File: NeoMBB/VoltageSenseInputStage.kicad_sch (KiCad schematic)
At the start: 8 parts

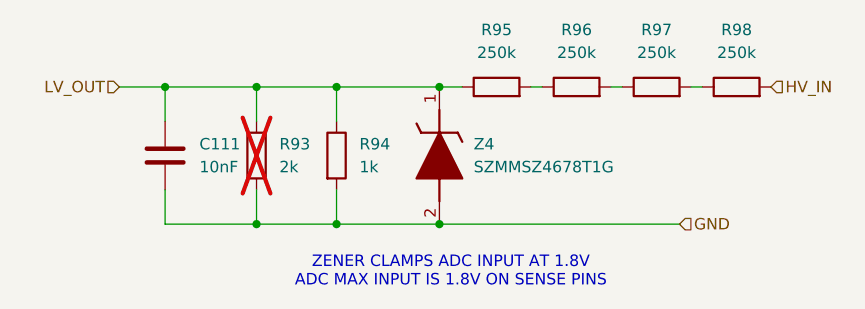
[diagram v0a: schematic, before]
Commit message: Probed Zero wiring harness
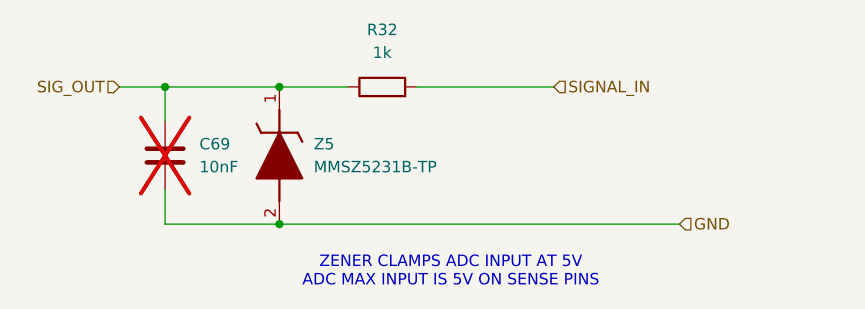
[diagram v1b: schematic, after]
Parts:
- removed R93: 2k, Resistor_SMD:R_1210_3225Metric_Pad1.30x2.65mm_HandSolder, symbol Device:R
- removed R95, R96, R97, R98: 250k, Resistor_SMD:R_1210_3225Metric_Pad1.30x2.65mm_HandSolder, symbol Device:R
- removed Z4: SZMMSZ4678T1G, InverterCom:SOD3716X135N, symbol InverterCom:SZMMSZ4678T1G
- added Z5: MMSZ5231B-TP, SOD3716X135N, symbol InverterCom:MMSZ5231B-TP
- C69: renamed from C111; now not fitted
- renumbered R94 to R32
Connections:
- net GND: now also Z5.2 (A); no longer R32.2
- net LV_OUT renamed SIG_OUT
- net SIG_OUT: now also Z5.1 (K)
- new net SIGNAL_IN: R32.2
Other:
- note added: "ZENER CLAMPS ADC INPUT AT 5V ADC MAX INPUT IS 5V ON SENSE PINS"
- note removed: "ZENER CLAMPS ADC INPUT AT 1.8V ADC MAX INPUT IS 1.8V ON SENSE PINS"
- moved on the sheet: R32
